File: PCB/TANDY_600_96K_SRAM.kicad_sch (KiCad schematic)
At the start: 5 parts

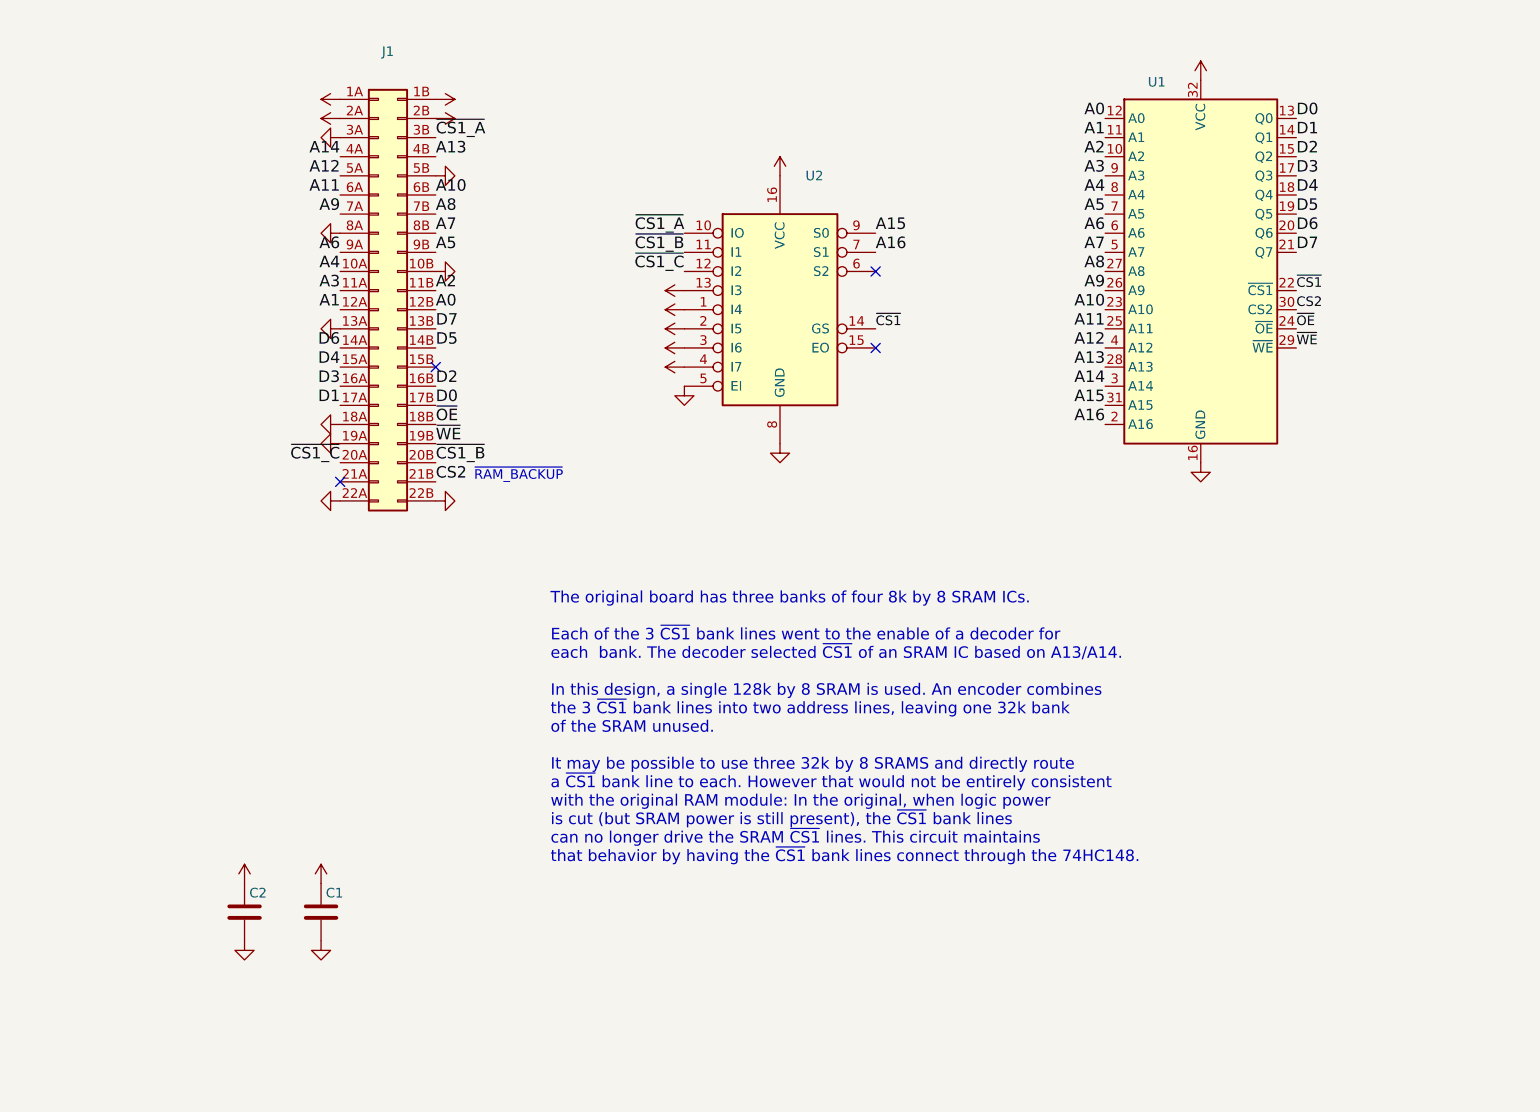
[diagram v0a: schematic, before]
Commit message: silkscreen, readme, pics
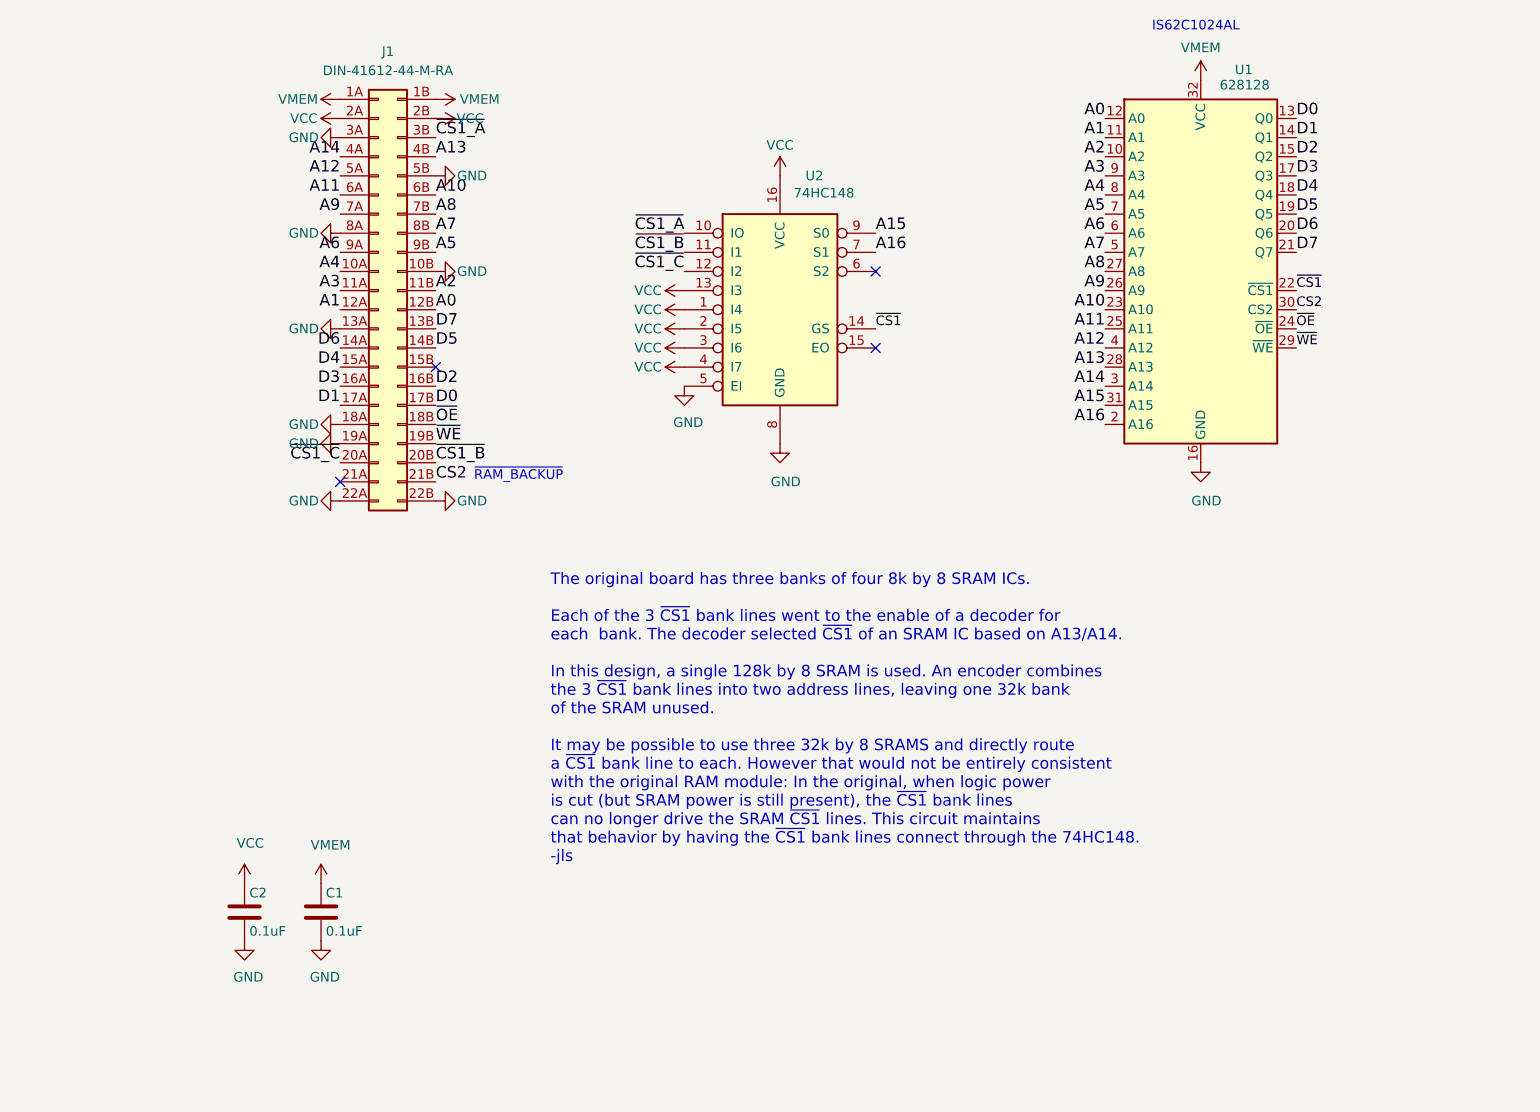
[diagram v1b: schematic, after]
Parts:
- C1, C2: value (none) -> 0.1uF; footprint (none) -> 000_LOCAL:C_1206
- J1: value (none) -> DIN-41612-44-M-RA; footprint (none) -> 000_LOCAL:DIN41612-44P-male-horiz
- U1: value (none) -> 628128; footprint (none) -> 000_LOCAL:SOP-32W
- U2: value (none) -> 74HC148; footprint (none) -> 000_LOCAL:SOIC-SOP-16
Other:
- note added: "IS62C1024AL"

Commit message: datasheets, update bom, teardrops on release gerbers
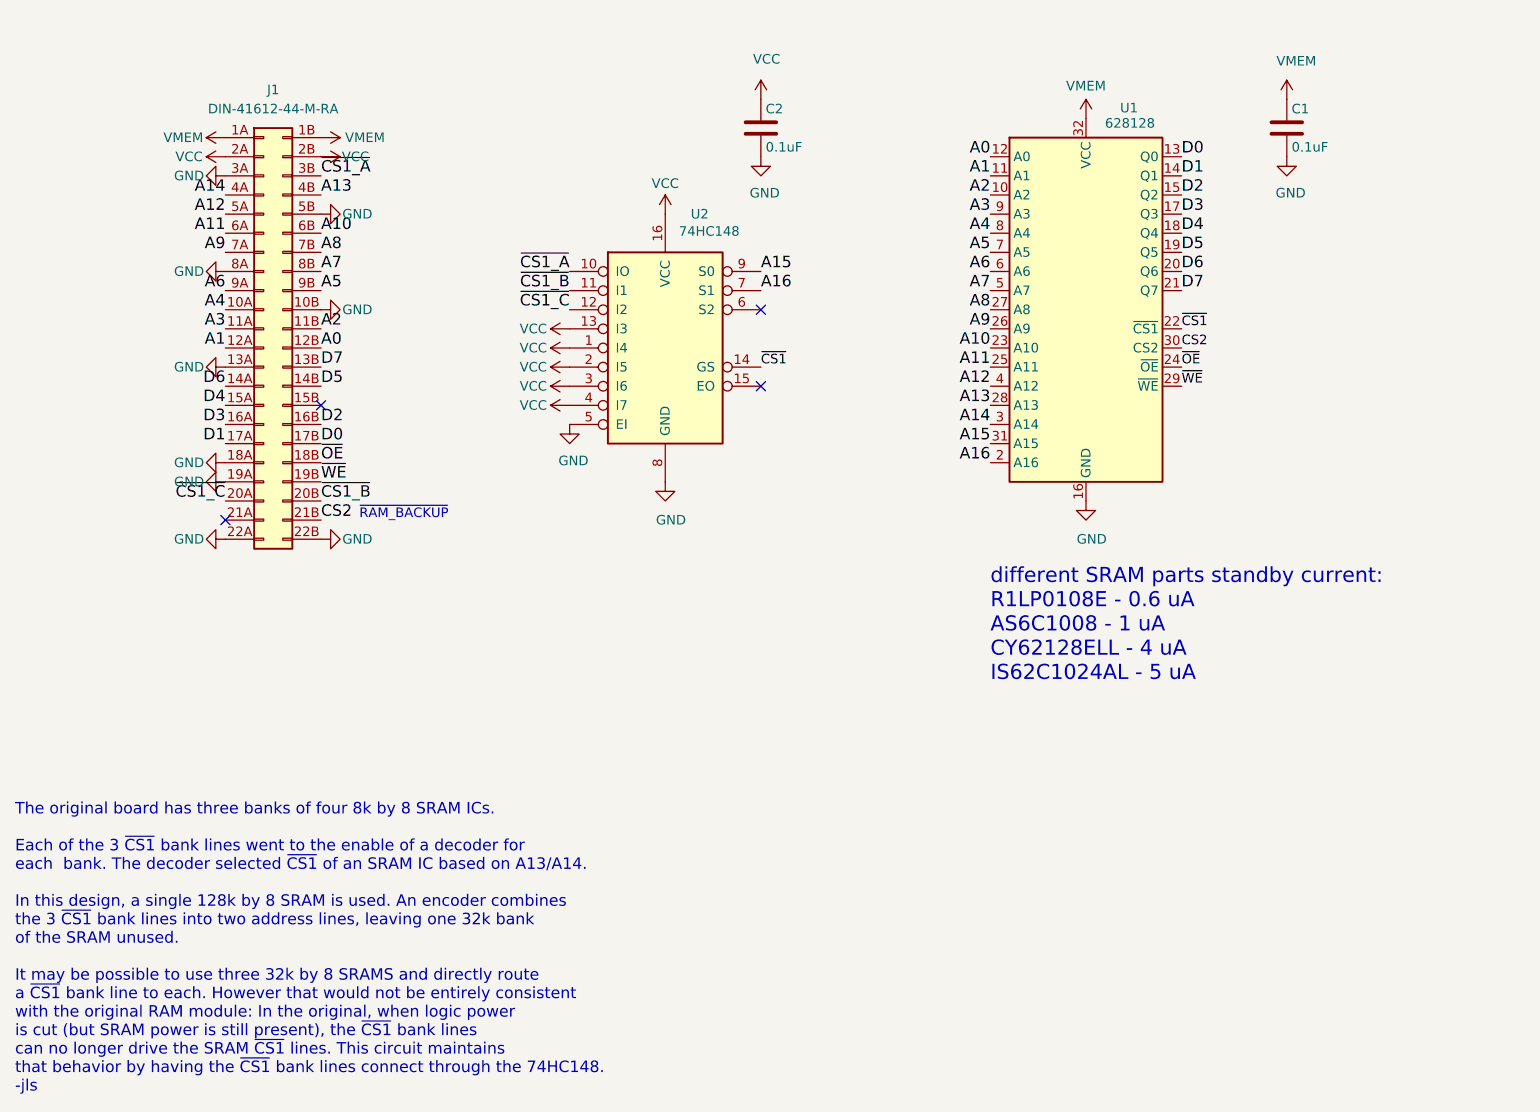
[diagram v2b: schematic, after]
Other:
- note added: "different SRAM parts standby current: R1LP0108E - 0.6 uA AS6C1008 - 1 uA CY62128ELL - 4 uA IS62C1024AL - 5 uA"
- note removed: "IS62C1024AL"
- moved on the sheet: C1, C2, J1, U1, U2
